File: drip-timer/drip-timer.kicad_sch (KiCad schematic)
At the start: 9 parts, among them J1 BATT, J2 VALVE, J3 FLASH, K1 DIPxx-1Axx-11x, SW1 GO, U1 ProMicro, U3 MOC3021

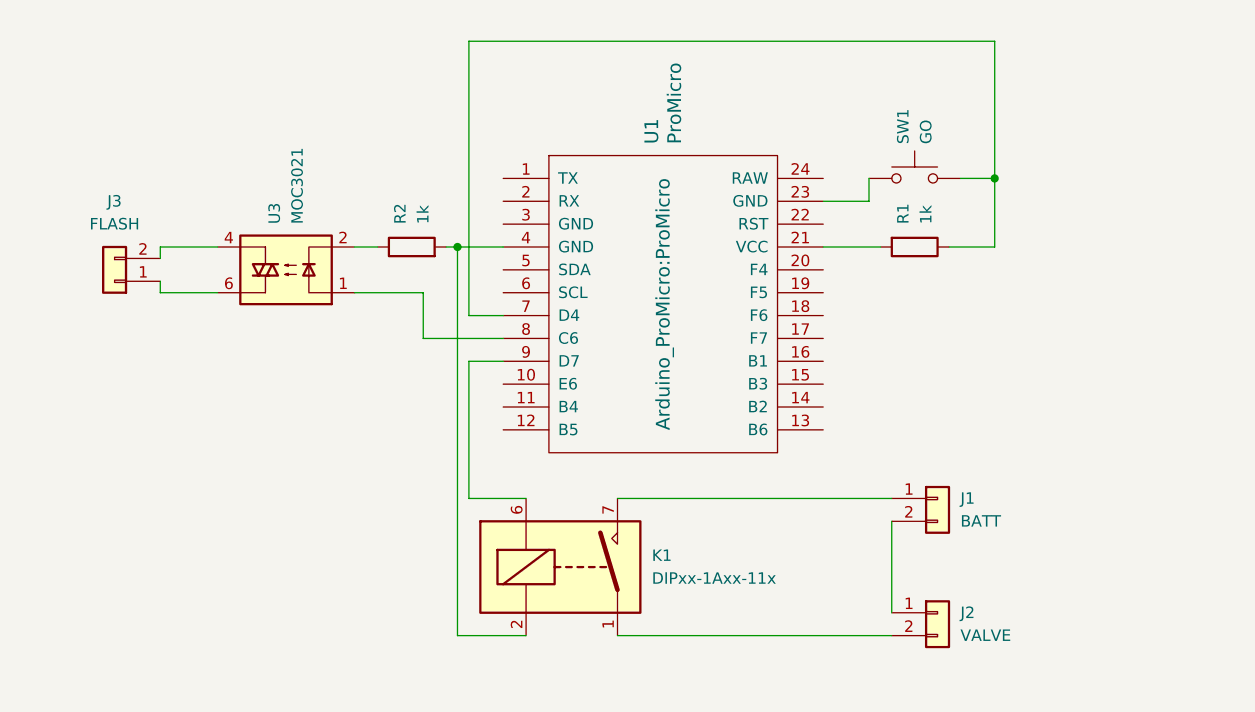
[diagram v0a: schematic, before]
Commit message: Add files via upload
Many updates, including switches and pots for better control, layout changes etc
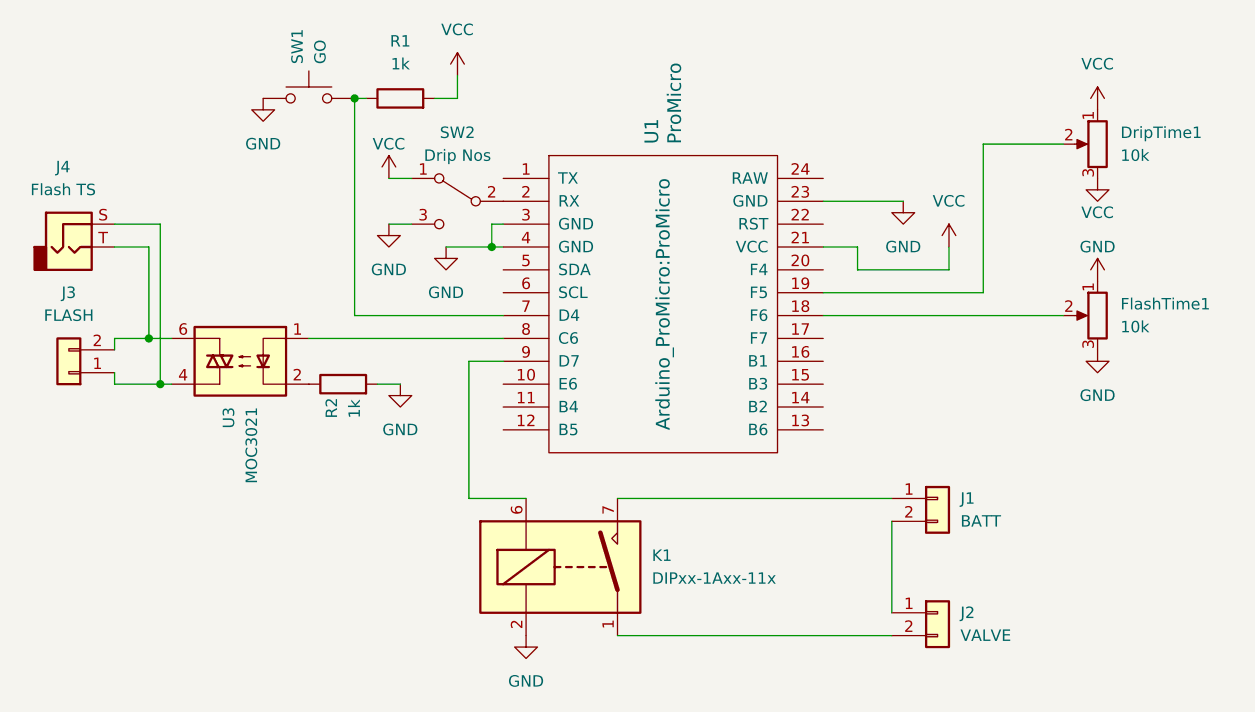
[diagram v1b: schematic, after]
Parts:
- added DripTime1, FlashTime1: 10k, Potentiometer_THT:Potentiometer_Bourns_PTV09A-1_Single_Vertical, symbol Device:R_Potentiometer
- added J4: Flash TS, Connector_Audio:Jack_3.5mm_CUI_SJ1-3523N_Horizontal, symbol Connector_Audio:AudioJack2
- added SW2: Drip Nos, symbol Switch:SW_SPDT
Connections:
- net at J3.1 (Pin_1): now also U3.4, J4.S; no longer U3.6
- net at J3.2 (Pin_2): now also U3.6, J4.T; no longer U3.4
- net VCC: now reaches R1.2, U1.21 (VCC)
- net VCC: now also DripTime1.1, FlashTime1.1, SW2.1 (A)
- net at U1.18 (F6): now also FlashTime1.2
- net at U1.19 (F5): now also DripTime1.2
- net at U1.2 (RX): now also SW2.2 (B)
- net GND: now reaches SW1.1, U1.23 (GND)
- net GND: now also K1.2, R2.2, U1.3 (GND), U1.4 (GND), DripTime1.3, FlashTime1.3, SW2.3 (C)
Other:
- moved on the sheet: J3, R1, R2, SW1, U3

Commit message: completed work on v0.1 of pcb
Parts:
- SW2: footprint (none) -> Button_Switch_THT:SW_E-Switch_EG1271_SPDT
- U3: value MOC3021 -> MOC3021S; footprint Package_DIP:Toshiba_11-7A9 -> Package_DIP:SMDIP-6_W7.62mm
